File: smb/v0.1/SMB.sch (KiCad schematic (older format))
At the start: 44 parts, among them IC1 MAX485, IC101 ATMEGA1284-A, IC2 DS2482-100S, J101 RJ45, J102 RTS_RESET, J103 ICSP, J104 SERIAL_REV, P101 I2C_CONN, P102 CONN_10X2, P103 CONN_5, P105 CONN_5, P107 CONN_3, P108 CONN_5, P109 CONN_3, P110 CONN_3, P112 CONN_2, P2 CONN_3, SW101 SKQGAKE010, X101 20MHz

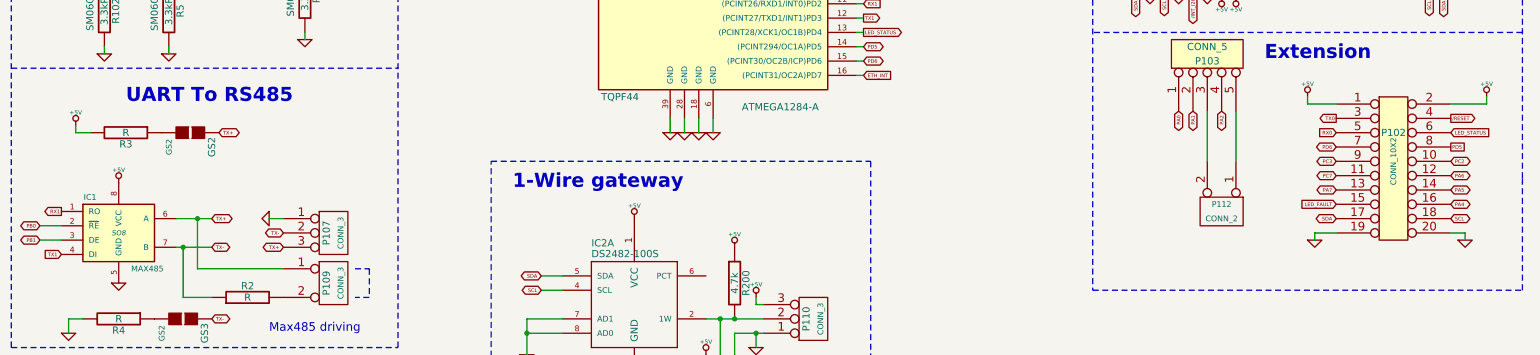
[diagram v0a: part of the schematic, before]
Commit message: Modification Routage SMB :         Connecteur Spare 3 broches avec GND         RX1 et TX1 sans via         Suppression via sur connexion vers front panel         Changement de place des nom pour le connecteur My Shield (Haut)         Modification du cable reset
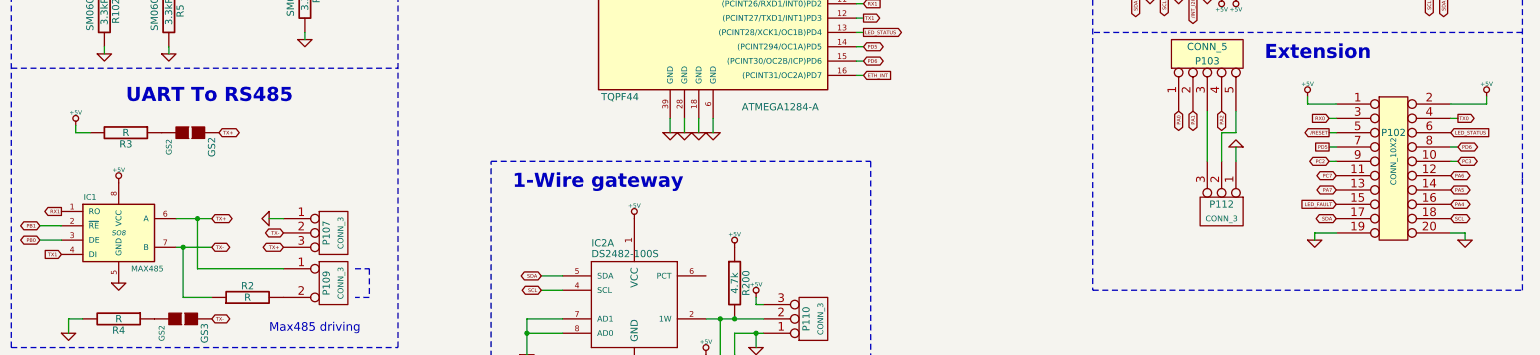
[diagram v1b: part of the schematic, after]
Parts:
- removed P112: CONN_2, symbol CONN_2
- added P112: CONN_3, symbol CONN_3
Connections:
- net /RESET: now also P102.5 (P5); no longer P102.4 (P4)
- net GND: now also P112.1 (P1)
- net PB0: now also IC1.3 (DE); no longer IC1.2 (~RE~)
- net PB1: now also IC1.2 (~RE~); no longer IC1.3 (DE)
- net PC2: now also P102.9 (P9); no longer P102.10 (P10)
- net PC3: now also P102.10 (P10); no longer P102.9 (P9)
- net PD5: now also P102.7 (P7); no longer P102.8 (P8)
- net PD6: now also P102.8 (P8); no longer P102.7 (P7)
- net RX0: now also P102.3 (P3); no longer P102.5 (P5)
- net TX0: now also P102.4 (P4); no longer P102.3 (P3)
- net at P103.3: now also P112.3 (P3)
- net at P103.5: now also P112.2 (PM)
